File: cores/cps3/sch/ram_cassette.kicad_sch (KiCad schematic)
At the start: 55 parts, among them U1 7400, U2 29F400TA-90PF, U3-SCU HD6417604F28_SH2, U4 7400, U6 FM1208S-250SC, X1 Crystal

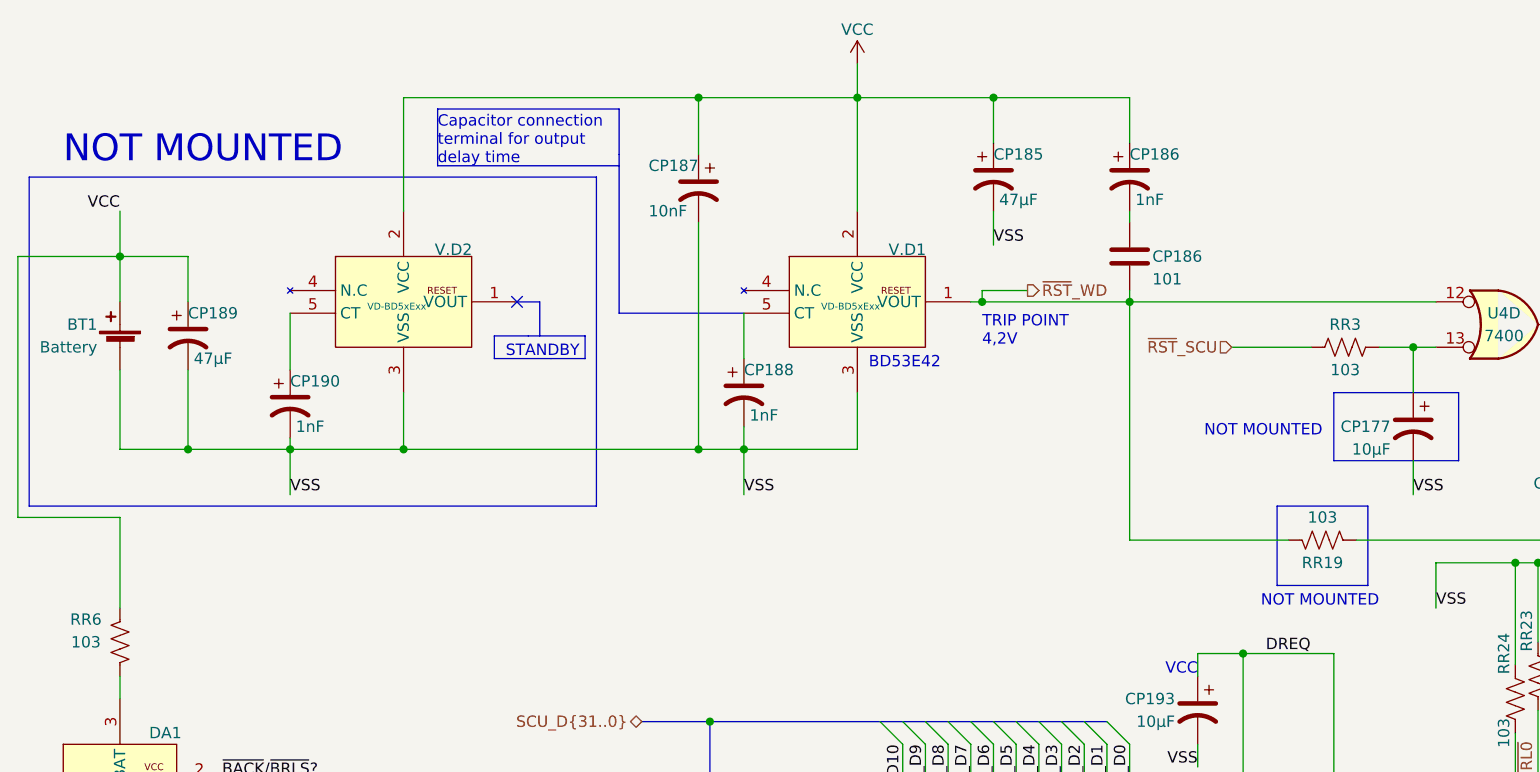
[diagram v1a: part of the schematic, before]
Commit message: sch: not mounted -> not populated
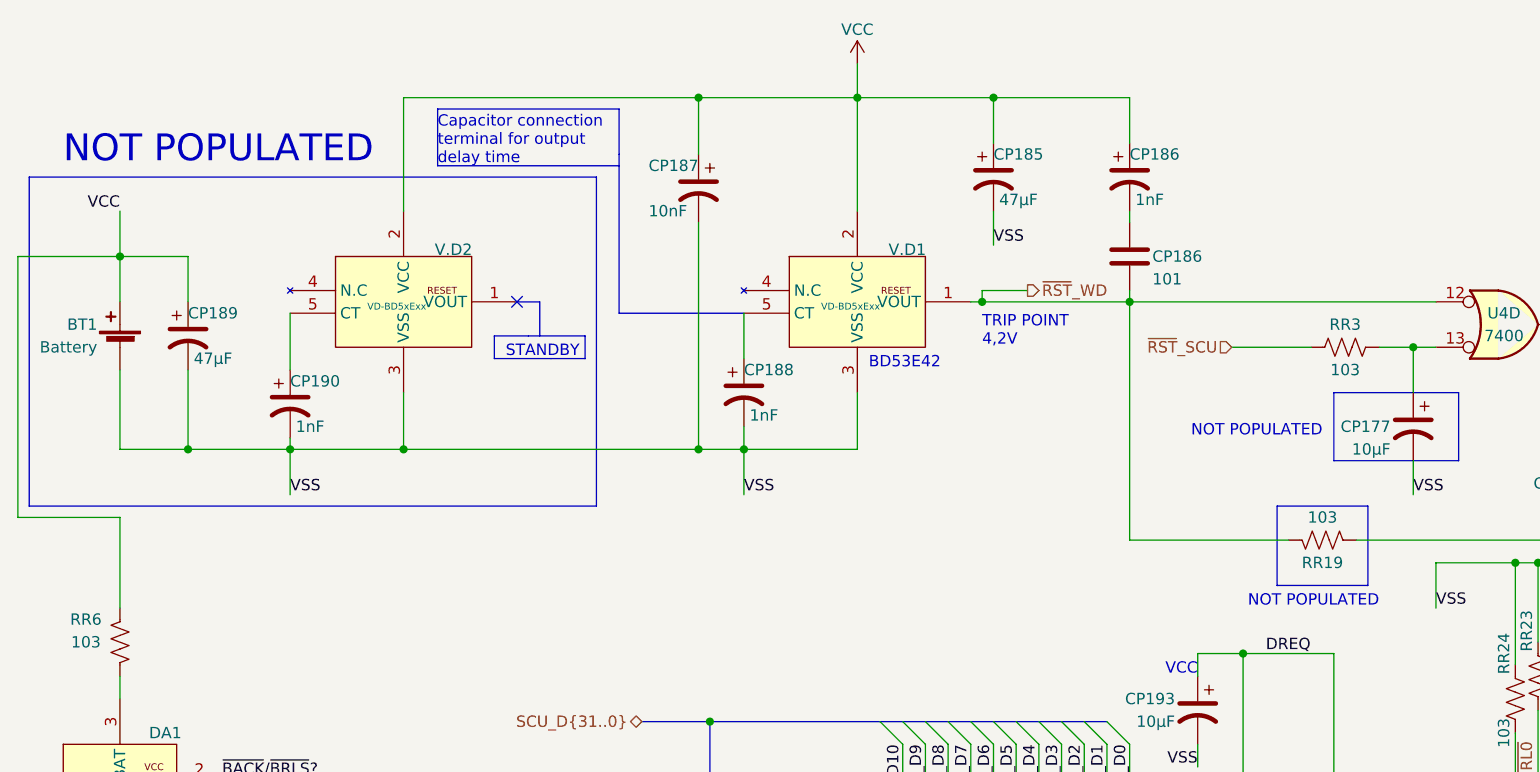
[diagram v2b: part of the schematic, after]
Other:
- note added: "NOT POPULATED"
- note removed: "NOT MOUNTED"
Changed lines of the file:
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@@
     (effects (font (size 1.27 1.27)) (justify left bottom))
   )
-  (text "NOT MOUNTED" (at 21.59 29.21 0)
+  (text "NOT POPULATED" (at 21.59 29.21 0)
     (effects (font (size 3 3)) (justify left bottom))
   )
@@
     (effects (font (size 1.27 1.27)) (justify left bottom))
   )
-  (text "NOT MOUNTED" (at 162.56 59.69 180)
+  (text "NOT POPULATED" (at 162.56 59.69 180)
     (effects (font (size 1.27 1.27)) (justify right bottom))
   )
-  (text "NOT MOUNTED" (at 168.91 78.74 180)
+  (text "NOT POPULATED" (at 168.91 78.74 180)
     (effects (font (size 1.27 1.27)) (justify right bottom))
   )
